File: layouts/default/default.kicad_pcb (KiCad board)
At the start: 2 copper layers, 38 parts

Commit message: Start work on battery pack
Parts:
- added C18: 100nF ±10% 50V X7R, YAGEO_CC0603KRX7R9BB104:C0603, F.Cu at (35.6, 92.1)
- added C19: 100nF ±10% 50V X7R, YAGEO_CC0603KRX7R9BB104:C0603, F.Cu at (35.6, 91.4)
- added C20: 100nF ±10% 50V X7R, YAGEO_CC0603KRX7R9BB104:C0603, F.Cu at (50.8, 73.7)
- added C21: 100nF ±10% 50V X7R, YAGEO_CC0603KRX7R9BB104:C0603, F.Cu at (43.2, 66.0)
- added C22: 100nF ±10% 50V X7R, YAGEO_CC0603KRX7R9BB104:C0603, F.Cu at (87.9, 111.5)
- added C23: 100nF ±10% 50V X7R, YAGEO_CC0603KRX7R9BB104:C0603, F.Cu at (97.9, 111.5)
- added C24: 470nF ±10% 25V X7R, Samsung_Electro_Mechanics_CL10B474KA8NNNC:C0603, F.Cu at (33.0, 120.1)
- added C25: 100nF ±10% 50V X7R, YAGEO_CC0603KRX7R9BB104:C0603, F.Cu at (43.0, 120.1)
- added C26: 100nF ±10% 50V X7R, YAGEO_CC0603KRX7R9BB104:C0603, F.Cu at (53.0, 120.1)
- added CN1: , XT30PW_M:CONN-TH_XT30PW-M, F.Cu at (22.9, 51.4)
- added CN2: , XT30PW_M:CONN-TH_XT30PW-M, F.Cu at (22.9, 78.7)
- added R16: 10Ω ±1% 100mW, UNI_ROYAL_0603WAF100JT5E:R0603, F.Cu at (23.6, 94.0)
- added R17: 10Ω ±1% 100mW, UNI_ROYAL_0603WAF100JT5E:R0603, F.Cu at (30.5, 91.4)
- added R18: 10Ω ±1% 100mW, UNI_ROYAL_0603WAF100JT5E:R0603, F.Cu at (23.6, 88.9)
- added R19: 10Ω ±1% 100mW, UNI_ROYAL_0603WAF100JT5E:R0603, F.Cu at (23.6, 68.6)
- added R20: 10Ω ±1% 100mW, UNI_ROYAL_0603WAF100JT5E:R0603, F.Cu at (23.6, 66.0)
- added R21: 10Ω ±1% 100mW, UNI_ROYAL_0603WAF100JT5E:R0603, F.Cu at (23.6, 63.5)
- added R22: 10Ω ±1% 100mW, UNI_ROYAL_0603WAF100JT5E:R0603, F.Cu at (63.0, 120.1)
- added R23: 10Ω ±1% 100mW, UNI_ROYAL_0603WAF100JT5E:R0603, F.Cu at (23.6, 96.5)
- added R24: 5mΩ ±1% 2W, TA_I_Tech_RLM25FEER005:R2512, F.Cu at (83.0, 120.1)
- added U2: , JST_Sales_America_B4B_XH_A_LF__SN:CONN-TH_B4B-XH-A-LF-SN, F.Cu at (17.8, 64.8)
- added U3: , JST_Sales_America_B4B_XH_A_LF__SN:CONN-TH_B4B-XH-A-LF-SN, F.Cu at (17.8, 92.7)
- added U4: , Texas_Instruments_BQ40Z80RSMR:VQFN-32_L4.0-W4.0-P0.40-TL-EP1.4, F.Cu at (70.5, 107.2)
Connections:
- net SRN renamed charger-SRN
- net gnd renamed -gnd

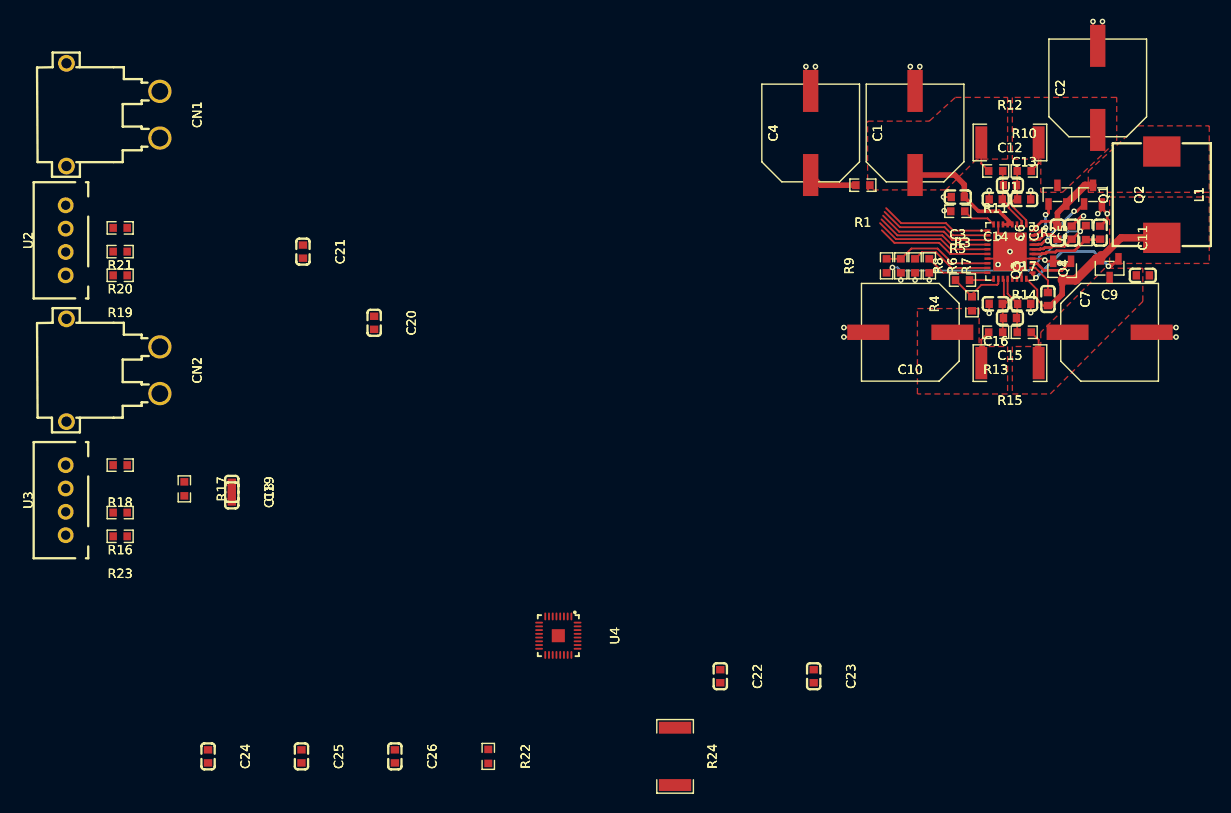
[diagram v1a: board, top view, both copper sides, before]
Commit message: Make a start on BQ40Z80
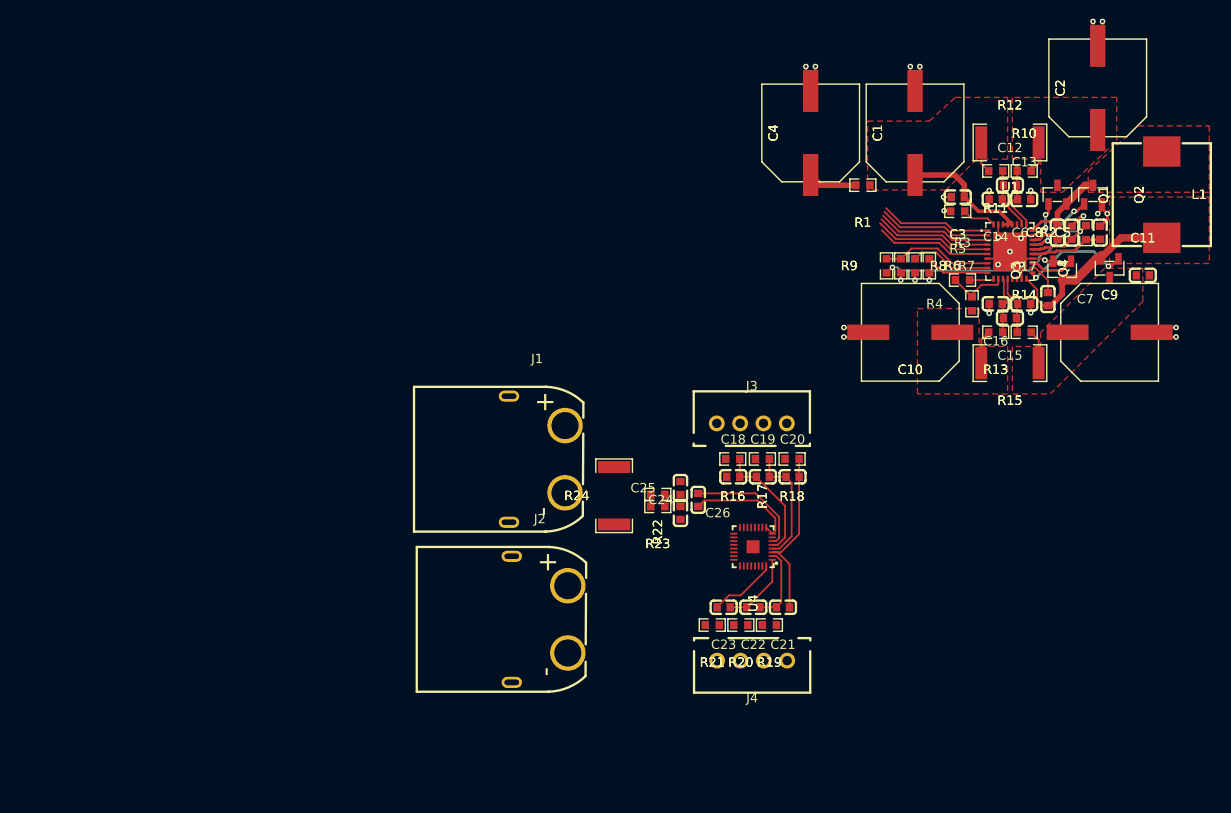
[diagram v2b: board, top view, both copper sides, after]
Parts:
- removed CN1, CN2: , XT30PW_M:CONN-TH_XT30PW-M
- removed U2, U3: , JST_Sales_America_B4B_XH_A_LF__SN:CONN-TH_B4B-XH-A-LF-SN
- added J1: , Changzhou_Amass_Elec_XT60PW_M:CONN-TH_XT60PW-M, F.Cu at (68.2, 88.3)
- added J2: , Changzhou_Amass_Elec_XT60PW_M:CONN-TH_XT60PW-M, F.Cu at (68.5, 105.4)
- added J3: , JST_Sales_America_B4B_XH_A_LF__SN:CONN-TH_B4B-XH-A-LF-SN, F.Cu at (91.2, 84.4)
- added J4: , JST_Sales_America_B4B_XH_A_LF__SN:CONN-TH_B4B-XH-A-LF-SN, F.Cu at (91.3, 109.8)
- moved R19 79.0 mm to (93.1, 106.0)
- moved R20 77.5 mm to (90.1, 106.0)
- moved R21 76.3 mm to (87.0, 106.0)
- moved R18 71.9 mm to (95.5, 88.2)
- moved R16 65.8 mm to (89.2, 88.2)
- moved C21 64.0 mm to (94.6, 104.1), turned to 180 degrees
- moved R17 62.0 mm to (92.4, 88.2), turned to 180 degrees
- moved C24 59.2 mm to (85.5, 92.6), turned to 90 degrees
- moved R23 57.6 mm to (81.2, 93.3)
- moved C19 56.9 mm to (92.4, 90.1), turned to 0 degrees
- moved C18 53.7 mm to (89.2, 90.1), turned to 0 degrees
- moved C25 49.7 mm to (83.6, 91.3), turned to 90 degrees
- moved C20 47.7 mm to (95.6, 90.1), turned to 0 degrees
- moved C26 40.2 mm to (83.6, 94.0)
- moved R22 33.4 mm to (81.2, 92.0), turned to 180 degrees
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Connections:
- R16 pad 2: pack-_3-1 -> pack-c1-0
- R17 pad 2: pack-_2-1 -> pack-c2-0
- R18 pad 2: pack-_4 -> pack-gnd-0
- R19 pad 2: pack-_4 -> pack-c1-1
- R20 pad 2: pack-_3-0 -> pack-c2-1
- R21 pad 2: pack-_2-0 -> vbat
- R23 pad 2: pack-gnd-0 -> pack-gnd-1
- R24 pad 1: pack-gnd-0 -> pack-gnd-1
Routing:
- net VC3: track 0.00 -> 18.7 mm
- net VC1: track 0.00 -> 13.1 mm
- net VC2: track 0.00 -> 12.9 mm
- net pack-SRN: track 0.00 -> 12.8 mm
- net vss: track 0.00 -> 12.0 mm
- net VC4: track 0.00 -> 8.11 mm
- net VC5: track 0.00 -> 7.99 mm
- net VC6: track 0.00 -> 7.33 mm

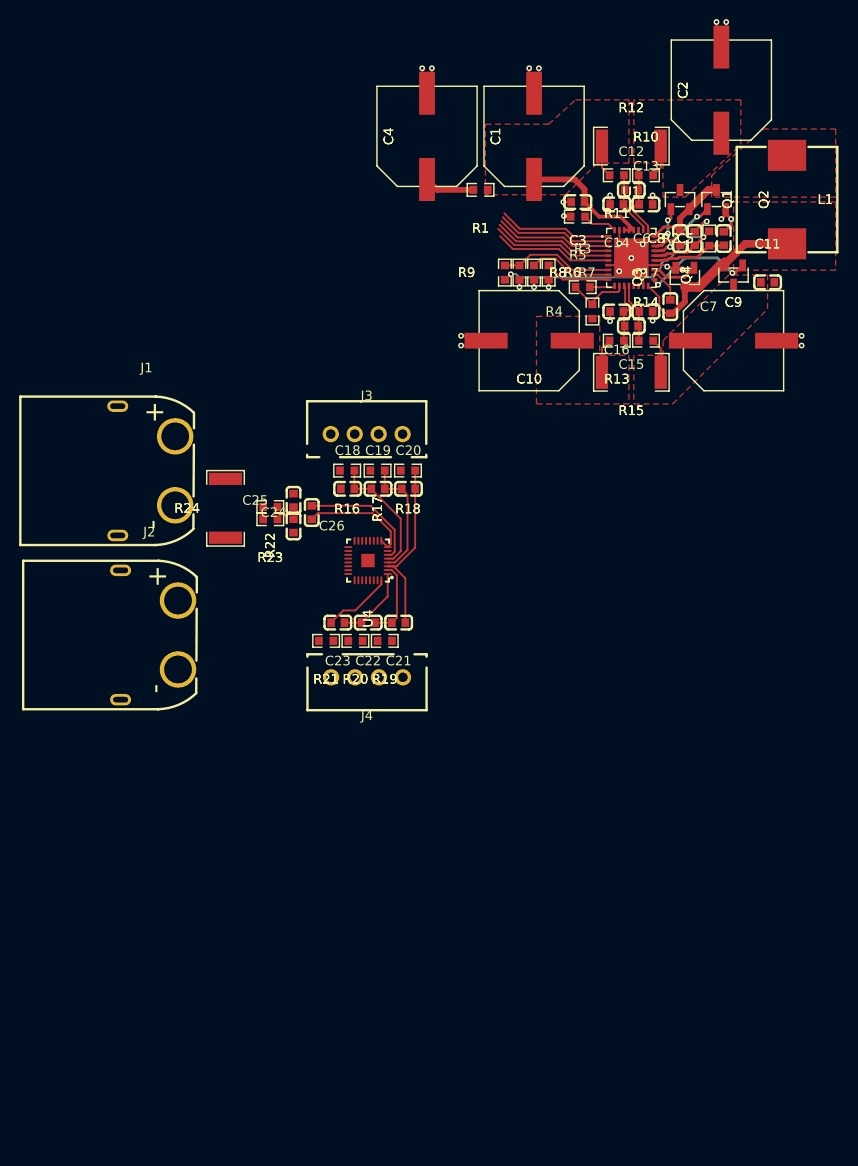
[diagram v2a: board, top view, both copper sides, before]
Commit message: Some work on the battery monitor
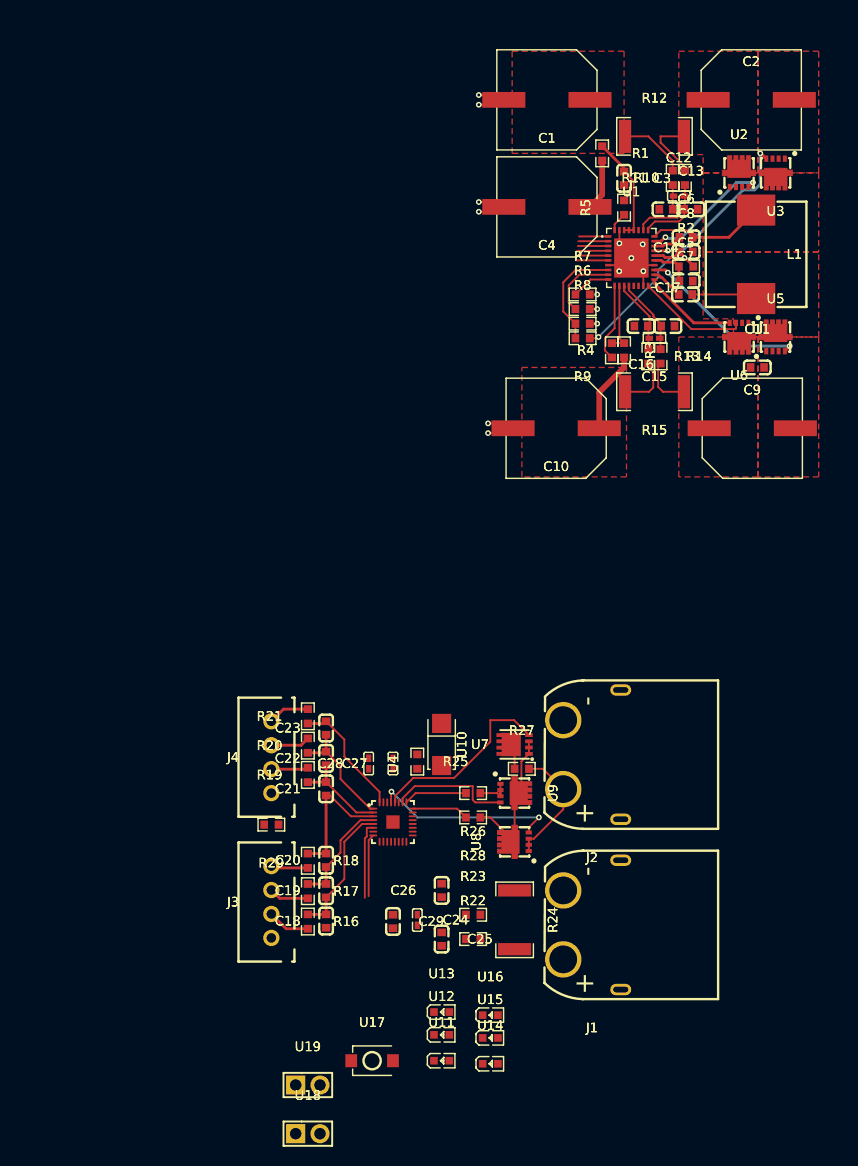
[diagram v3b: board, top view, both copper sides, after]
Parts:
- removed Q1, Q2, Q3, Q4: , Alpha___Omega_Semicon_AO3400A:SOT-23-3_L2.9-W1.3-P1.90-LS2.4-BR
- added C27: 100pF ±5% 50V C0G, FH_0402CG101J500NT:C0402, F.Cu at (94.0, 118.8)
- added C28: 100pF ±5% 50V C0G, FH_0402CG101J500NT:C0402, F.Cu at (91.4, 118.8)
- added C29: 100nF ±10% 50V X7R, YAGEO_CC0603KRX7R9BB104:C0603, F.Cu at (94.0, 135.3)
- added R25: 10Ω ±1% 100mW, UNI_ROYAL_0603WAF100JT5E:R0603, F.Cu at (96.5, 118.6)
- added R26: 10kΩ ±1% 100mW, UNI_ROYAL_0603WAF1002T5E:R0603, F.Cu at (102.3, 121.9)
- added R27: 1kΩ ±1% 100mW, UNI_ROYAL_0603WAF1001T5E:R0603, F.Cu at (107.4, 119.4)
- added R28: 100Ω ±1% 100mW, UNI_ROYAL_0603WAF1000T5E:R0603, F.Cu at (102.3, 124.5)
- added R29: 0Ω 100mW, UNI_ROYAL_0603WAF0000T5E:R0603, F.Cu at (81.3, 125.2)
- added U10: , XNRUSEMI_XR15P06D:DFN-8_L3.0-W3.0-P0.65-BL-4, F.Cu at (106.7, 116.8)
- added U11: , Hubei_KENTO_Elec_KT_0603R:LED0603-RD, F.Cu at (99.1, 149.9)
- added U12: , Hubei_KENTO_Elec_KT_0603R:LED0603-RD, F.Cu at (99.1, 147.2)
- added U13: , Hubei_KENTO_Elec_KT_0603R:LED0603-RD, F.Cu at (99.1, 144.8)
- added U14: , Hubei_KENTO_Elec_KT_0603R:LED0603-RD, F.Cu at (104.1, 150.2)
- added U15: , Hubei_KENTO_Elec_KT_0603R:LED0603-RD, F.Cu at (104.1, 147.5)
- added U16: , Hubei_KENTO_Elec_KT_0603R:LED0603-RD, F.Cu at (104.1, 145.1)
- added U17: , XUNPU_TS_1088_AR02016:SW-SMD_L3.9-W3.0-P4.45, F.Cu at (91.8, 149.9)
- added U18: , XFCN_PZ254V_11_02P:HDR-TH_2P-P2.54-V-M, F.Cu at (85.1, 157.5)
- added U19: , XFCN_PZ254V_11_02P:HDR-TH_2P-P2.54-V-M, F.Cu at (85.1, 152.4)
- added U2: , HL_40N06D:WDFN-5_L3.3-W3.3-P0.65-BL, F.Cu at (130.1, 57.9)
- added U3: , HL_40N06D:WDFN-5_L3.3-W3.3-P0.65-BL, F.Cu at (133.9, 56.4)
- added U5: , HL_40N06D:WDFN-5_L3.3-W3.3-P0.65-BL, F.Cu at (133.9, 75.0)
- added U6: , HL_40N06D:WDFN-5_L3.3-W3.3-P0.65-BL, F.Cu at (130.1, 73.6)
- added U7: , MDD_Microdiode_Electronics_SS34:SMA_L4.3-W2.6-LS5.2-RD, F.Cu at (99.1, 116.8)
- added U8: , HL_40N06D:WDFN-5_L3.3-W3.3-P0.65-BL, F.Cu at (107.4, 127.0)
- added U9: , HL_40N06D:WDFN-5_L3.3-W3.3-P0.65-BL, F.Cu at (105.9, 121.9)
- C12, C15: value 470nF ±10% 25V X7R -> 470nF ±20% 16V X5R; footprint Samsung_Electro_Mechanics_CL10B474KA8NNNC:C0603 -> CCTC_TCC0402X5R474M160AT:C0402
- C24: value 470nF ±10% 25V X7R -> 100pF ±5% 50V C0G; footprint Samsung_Electro_Mechanics_CL10B474KA8NNNC:C0603 -> FH_0402CG101J500NT:C0402
- R24: value 5mΩ ±1% 2W -> 1mΩ ±1% 3W; footprint TA_I_Tech_RLM25FEER005:R2512 -> Milliohm_HoYLR2512E_3W_1mR_1:R2512
- moved J1 66.4 mm to (114.8, 135.7), turned to 180 degrees
- moved R24 52.5 mm to (106.7, 135.2), turned to -90 degrees
- moved J3 49.9 mm to (81.3, 133.3), turned to 90 degrees
- moved R22 49.8 mm to (102.3, 137.2), turned to 0 degrees
- moved C25 48.4 mm to (99.1, 137.2), turned to -90 degrees
- moved J2 47.9 mm to (114.8, 117.9), turned to 180 degrees
- moved R16 47.3 mm to (85.1, 135.3), turned to -90 degrees
- moved R23 46.4 mm to (102.3, 134.6), turned to 0 degrees
- moved C18 45.2 mm to (87.0, 135.3), turned to 90 degrees
- moved R17 44.5 mm to (85.1, 132.2), turned to -90 degrees
- moved C24 44.0 mm to (96.5, 135.2), turned to -90 degrees
- moved C19 42.3 mm to (87.0, 132.1), turned to 90 degrees
- moved R18 42.1 mm to (85.1, 129.0), turned to -90 degrees
- moved C26 41.1 mm to (99.1, 132.1), turned to 90 degrees
- moved C20 39.7 mm to (87.0, 128.9), turned to 90 degrees
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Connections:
- net SRP renamed charger-SRP
- net anode renamed charger-anode
- net charger-D-1 renamed charger-D
- net pgnd renamed pack_n
- C11 pad 1: charger-pos-2 -> charger-pos-3
- C2 pad 1: charger-D-0 -> charger-pos-1
- C24 pad 1: vss -> pack-SRP
- C25 pad 2: pack.sense-gnd -> -gnd
- C26 pad 1: vss -> pack-SRP
- C26 pad 2: pack.sense-gnd -> -gnd
- C4 pad 1: charger-pos-1 -> charger-pos-2
- C9 pad 1: charger-pos-2 -> charger-pos-3
- J1 pad 1: pack-gnd-1 -> -gnd
- J1 pad 2: pack-gnd-2 -> pack-gnd-1
- J2 pad 1: pack-gnd-2 -> pack-gnd-1
- J3 pad 1: pack-gnd-0 -> c3
- J3 pad 4: pack-gnd-1 -> -gnd
- R1 pad 2: charger-pos-1 -> charger-pos-2
- R10 pad 2: charger-D-0 -> charger-pos-1
- R12 pad 2: charger-D-0 -> charger-pos-1
- R14 pad 2: charger-pos-2 -> charger-pos-3
- R15 pad 1: charger-pos-2 -> charger-pos-3
- R18 pad 2: pack-gnd-0 -> c3
- R23 pad 1: vss -> pack-SRP
- R23 pad 2: pack-gnd-1 -> -gnd
- R24 pad 1: pack-gnd-1 -> -gnd
- U4 pad 20: LEDCNTLA_PDSG_GPIO -> pack-anode
- U4 pad 21: LEDCNTLB_GPIO -> pack-cathode-1
- U4 pad 22: LEDCNTLC_GPIO -> pack-cathode-2
- U4 pad 23: FUSE -> -gnd
- U4 pad 33: EP -> -gnd
- U4 pad 8: vss -> pack-SRP
- U4 pad 9: vss -> -gnd
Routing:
- net -gnd: track 57.5 -> 30.8 mm, vias 29 -> 14
- net PCHG: track 0.00 -> 19.9 mm
- net CHG: track 0.00 -> 19.7 mm, vias 0 -> 2
- net vbat: track 0.00 -> 17.1 mm
- net pack-D-0: track 0.00 -> 15.7 mm
- net charger-G-3: track 4.85 -> 18.2 mm, vias 0 -> 2
- net DSG: track 0.00 -> 12.7 mm
- net vss: track 12.0 -> 0.00 mm
- net REGN: track 29.8 -> 18.9 mm
- net vsys: track 3.63 -> 14.3 mm
- net charger-G-2: track 7.54 -> 18.0 mm
- net STAT2: track 12.7 -> 3.32 mm
- net STAT1: track 12.5 -> 3.26 mm
- net charger-G-0: track 4.49 -> 13.6 mm
- net nINT: track 12.3 -> 3.19 mm
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- added copper zone on F.Cu, net -gnd
- added copper zone on F.Cu, net charger-pos-1
- added copper zone on F.Cu, net charger-pos-3
- removed copper zone on F.Cu, net charger-D-0
- removed copper zone on F.Cu, net charger-pos-2

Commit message: Some more work on fuel gauge
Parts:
- added C30: 2.2µF ±20% 6.3V X5R, Samsung_Electro_Mechanics_CL05A225MQ5NSNC:C0402, F.Cu at (91.4, 114.3)
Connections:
- net c3 renamed pack-c3-0
- J4 pad 1: vbat -> pack-c3-1
- R21 pad 2: vbat -> pack-c3-1
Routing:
- net vbat: track 17.1 -> 12.7 mm
- net pack-c3-1: track 0.00 -> 4.34 mm

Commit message: Uh. Stuff
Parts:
- added R30: 10MΩ ±1% 100mW, YAGEO_RC0603FR_0710ML:R0603, F.Cu at (0.00, -40.0)
- added R31: 10MΩ ±1% 100mW, YAGEO_RC0603FR_0710ML:R0603, F.Cu at (0.00, -50.0)
- added U20: , XNRUSEMI_XR15P06D:DFN-8_L3.0-W3.0-P0.65-BL-4, F.Cu at (0.00, -30.0)
- C24, C27, C28: footprint FH_0402CG101J500NT:C0402 -> Samsung_Electro_Mechanics_CL10C101JB8NNNC:C0603
- R25: value 10Ω ±1% 100mW -> 100Ω ±1% 100mW; footprint UNI_ROYAL_0603WAF100JT5E:R0603 -> UNI_ROYAL_0603WAF1000T5E:R0603
- R26: value 10kΩ ±1% 100mW -> 10kΩ ±1% 62.5mW; footprint UNI_ROYAL_0603WAF1002T5E:R0603 -> UNI_ROYAL_0402WGF1002TCE:R0402
- U10: footprint XNRUSEMI_XR15P06D:DFN-8_L3.0-W3.0-P0.65-BL-4 -> HL_40N06D:WDFN-5_L3.3-W3.3-P0.65-BL
- U8: footprint HL_40N06D:WDFN-5_L3.3-W3.3-P0.65-BL -> MDD_Microdiode_Electronics_SS34:SMA_L4.3-W2.6-LS5.2-RD
- moved U10 173.5 mm to (0.00, -20.0), turned to 0 degrees
- moved U9 169.2 mm to (0.00, -10.0), turned to 0 degrees
- moved U8 166.3 mm to (0.00, 0.00), turned to 0 degrees
- moved C30 4.33 mm to (91.8, 118.6)
- moved C28 1.79 mm to (93.2, 118.6)
- moved C27 0.91 mm to (94.9, 118.6)
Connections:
- C25 pad 2: -gnd -> pack-gnd-1
- C26 pad 2: -gnd -> pack-gnd-1
- J1 pad 1: -gnd -> pack-gnd-1
- J1 pad 2: pack-gnd-1 -> pack-gnd-2
- J2 pad 1: pack-gnd-1 -> pack-gnd-2
- U10 pad 1: pack-D-0 -> pack_p
- U10 pad 2: pack-D-0 -> pack_p
- U10 pad 3: pack-D-0 -> pack_p
- U10 pad 4: PCHG -> DSG
- U10 pad 5: pack-D-1 -> pack-D-0
- U8 pad 1: vbat -> pack.d_qdsg-cathode
- U8 pad 2: vbat -> pack.d_qdsg-anode
- U9 pad 1: pack_p -> vbat
- U9 pad 2: pack_p -> vbat
- U9 pad 3: pack_p -> vbat
- U9 pad 4: DSG -> CHG
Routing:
- net (no net): track 0.00 -> 87.6 mm, vias 0 -> 2
- net PCHG: track 19.9 -> 0.00 mm
- net CHG: track 19.7 -> 0.00 mm, vias 2 -> 0
- net pack-D-0: track 15.7 -> 0.00 mm
- net vbat: track 12.7 -> 0.00 mm
- net DSG: track 12.7 -> 0.00 mm
- net pack_p: track 4.16 -> 0.00 mm
- net pack-D-1: track 2.68 -> 0.00 mm
